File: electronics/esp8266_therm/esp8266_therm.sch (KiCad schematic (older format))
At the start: 20 parts, among them J1 CONN_01X02, J2 CONN_01X03, J3 CONN_01X03, J4 CONN_01X02, J5 CONN_01X08, J6 CONN_01X08, J7 CONN_01X02, J8 CONN_01X06, M1 BMP180_Breakout, Q1 Q_PMOS_GSD, SW1 SW_SPST, SW2 SW_SPST, U1 ESP-12E, U2 MCP1703A-3302/MB

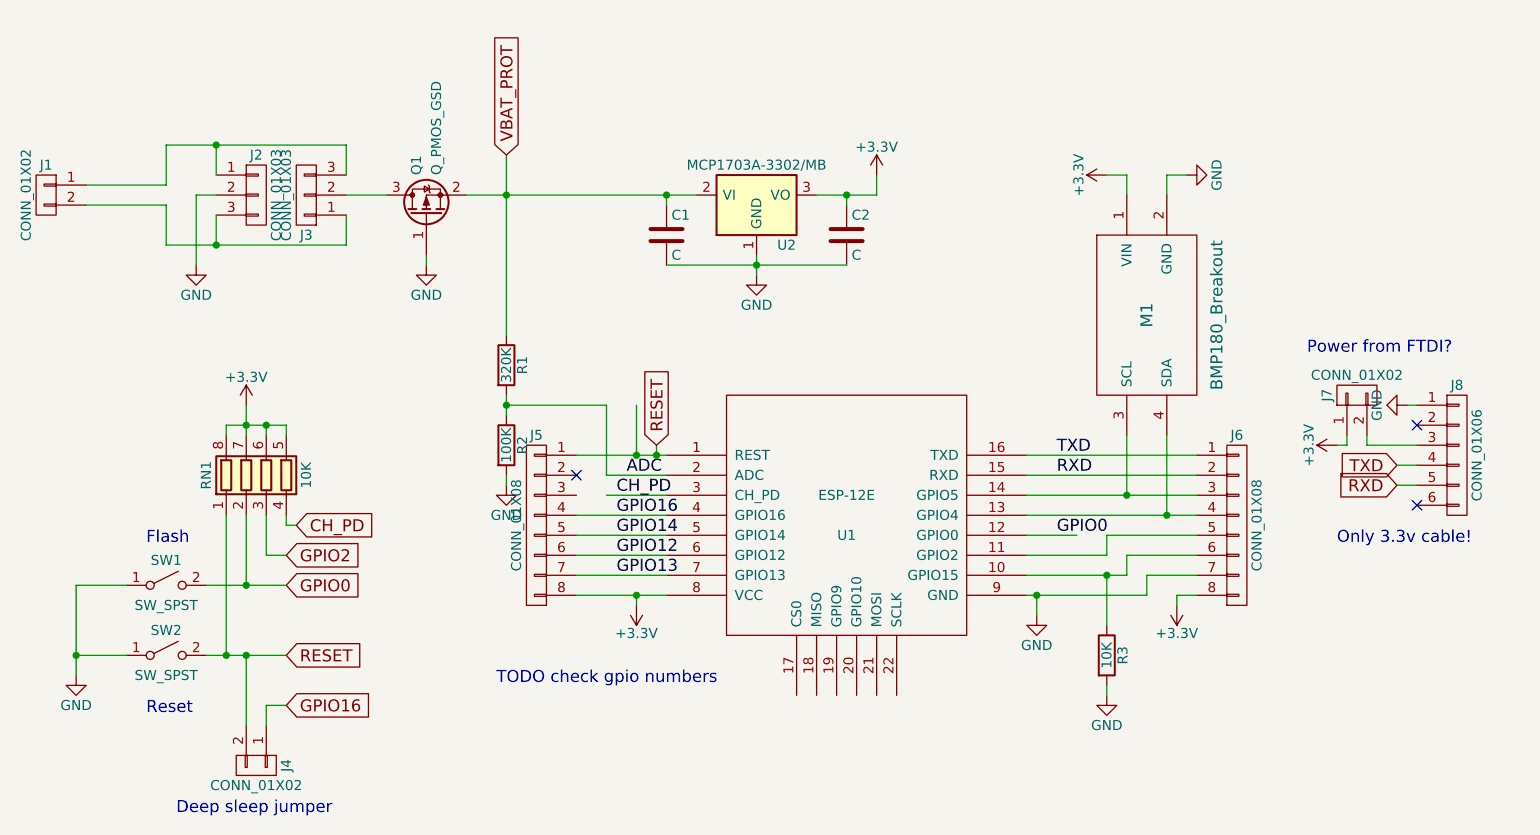
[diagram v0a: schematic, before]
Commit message: Update pinout on board to match D1 mini
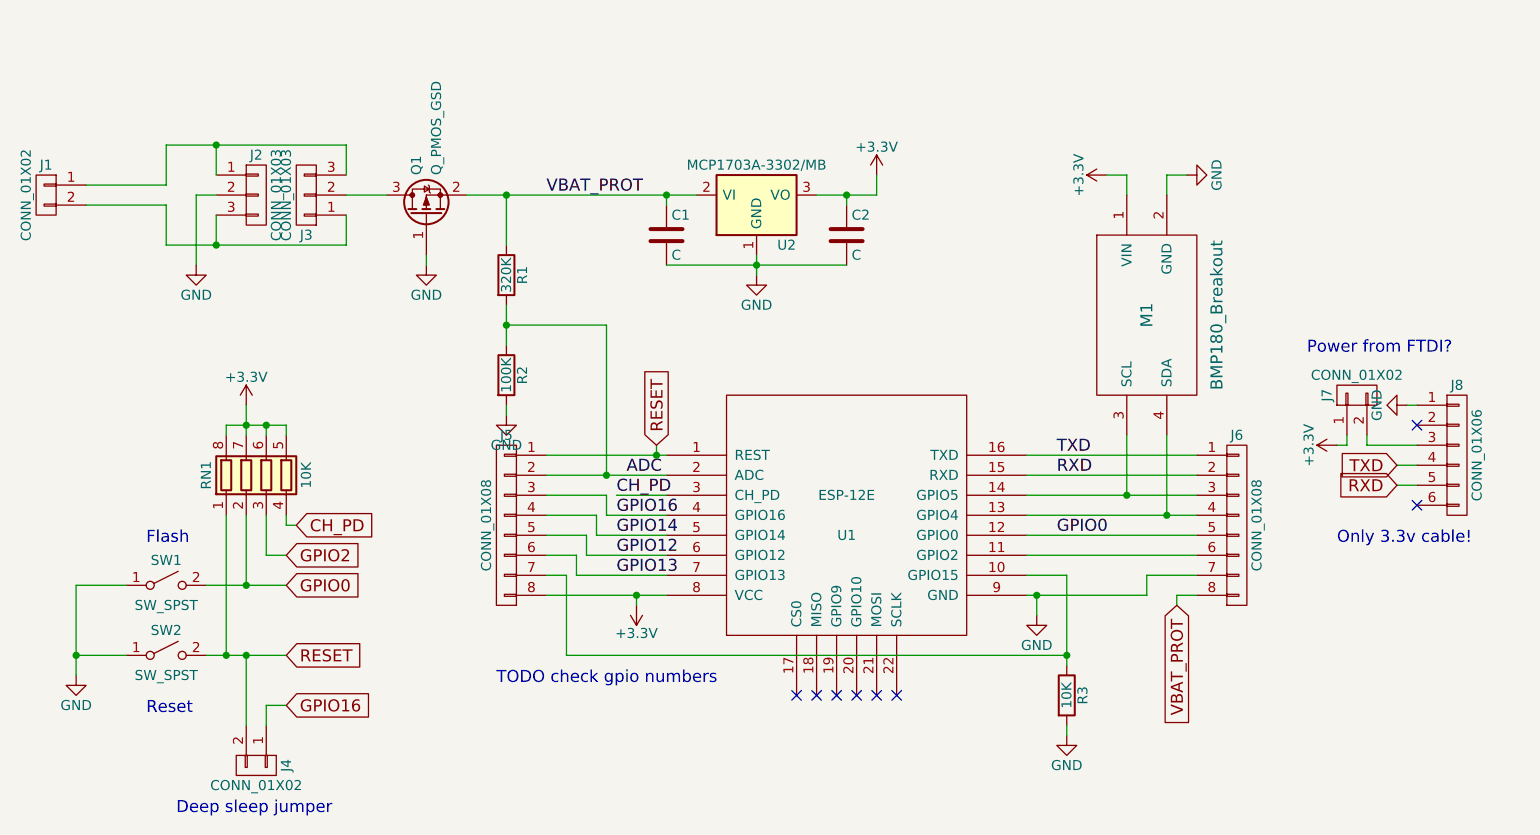
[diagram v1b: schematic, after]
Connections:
- wire segments 88 -> 94
- no-connect marks 3 -> 8
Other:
- moved on the sheet: J5, R1, R2, R3
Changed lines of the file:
@@
 L R R1
 U 1 1 5960122C
-P 5150 3600
-F 0 "R1" V 5230 3600 50  0000 C CNN
-F 1 "320K" V 5150 3600 50  0000 C CNN
-F 2 "Resistors_SMD:R_0603_HandSoldering" V 5080 3600 50  0001 C CNN
-F 3 "" H 5150 3600 50  0001 C CNN
-	1    5150 3600
+P 5150 3150
+F 0 "R1" V 5230 3150 50  0000 C CNN
+F 1 "320K" V 5150 3150 50  0000 C CNN
+F 2 "Resistors_SMD:R_0603_HandSoldering" V 5080 3150 50  0001 C CNN
+F 3 "" H 5150 3150 50  0001 C CNN
+	1    5150 3150
 	1    0    0    -1
 $EndComp
@@
 L R R2
 U 1 1 59601270
-P 5150 4000
-F 0 "R2" V 5230 4000 50  0000 C CNN
-F 1 "100K" V 5150 4000 50  0000 C CNN
-F 2 "Resistors_SMD:R_0603_HandSoldering" V 5080 4000 50  0001 C CNN
-F 3 "" H 5150 4000 50  0001 C CNN
-	1    5150 4000
+P 5150 3650
+F 0 "R2" V 5230 3650 50  0000 C CNN
+F 1 "100K" V 5150 3650 50  0000 C CNN
+F 2 "Resistors_SMD:R_0603_HandSoldering" V 5080 3650 50  0001 C CNN
+F 3 "" H 5150 3650 50  0001 C CNN
+	1    5150 3650
 	1    0    0    -1
 $EndComp
@@
 L GND #PWR07
 U 1 1 596012FB
-P 5150 4200
-F 0 "#PWR07" H 5150 3950 50  0001 C CNN
-F 1 "GND" H 5150 4050 50  0000 C CNN
-F 2 "" H 5150 4200 50  0001 C CNN
-F 3 "" H 5150 4200 50  0001 C CNN
-	1    5150 4200
+P 5150 3850
+F 0 "#PWR07" H 5150 3600 50  0001 C CNN
+F 1 "GND" H 5150 3700 50  0000 C CNN
+F 2 "" H 5150 3850 50  0001 C CNN
+F 3 "" H 5150 3850 50  0001 C CNN
+	1    5150 3850
 	1    0    0    -1
 $EndComp
@@
 L CONN_01X08 J5
 U 1 1 59602C27
-P 5300 4400
-F 0 "J5" H 5300 4850 50  0000 C CNN
-F 1 "CONN_01X08" V 5400 4400 50  0000 C CNN
-F 2 "Pin_Headers:Pin_Header_Straight_1x08_Pitch2.54mm" H 5300 4400 50  0001 C CNN
-F 3 "" H 5300 4400 50  0001 C CNN
-	1    5300 4400
+P 5150 4400
+F 0 "J5" H 5150 4850 50  0000 C CNN
+F 1 "CONN_01X08" V 5250 4400 50  0000 C CNN
+F 2 "Pin_Headers:Pin_Header_Straight_1x08_Pitch2.54mm" H 5150 4400 50  0001 C CNN
+F 3 "" H 5150 4400 50  0001 C CNN
+	1    5150 4400
 	-1   0    0    -1
 $EndComp
@@
 	1    0    0    -1
 $EndComp
-$Comp
-L +3.3V #PWR011
-U 1 1 59603692
-P 8500 4800
-F 0 "#PWR011" H 8500 4650 50  0001 C CNN
-F 1 "+3.3V" H 8500 4940 50  0000 C CNN
-F 2 "" H 8500 4800 50  0001 C CNN
-F 3 "" H 8500 4800 50  0001 C CNN
-	1    8500 4800
-	-1   0    0    1
-$EndComp
 Text Notes 3350 5350 0    60   ~ 0
 Reset
@@
 $EndComp
 $Comp
-L GND #PWR012
+L GND #PWR011
 U 1 1 59604130
 P 9650 3800
-F 0 "#PWR012" H 9650 3550 50  0001 C CNN
+F 0 "#PWR011" H 9650 3550 50  0001 C CNN
 F 1 "GND" H 9650 3650 50  0000 C CNN
 F 2 "" H 9650 3800 50  0001 C CNN
@@
 $EndComp
 $Comp
-L +3.3V #PWR013
+L +3.3V #PWR012
 U 1 1 5960417A
 P 9300 4000
-F 0 "#PWR013" H 9300 3850 50  0001 C CNN
+F 0 "#PWR012" H 9300 3850 50  0001 C CNN
 F 1 "+3.3V" H 9300 4140 50  0000 C CNN
 F 2 "" H 9300 4000 50  0001 C CNN
@@
 RXD
 $Comp
-L +3.3V #PWR014
+L +3.3V #PWR013
 U 1 1 5960556B
 P 3850 3800
-F 0 "#PWR014" H 3850 3650 50  0001 C CNN
+F 0 "#PWR013" H 3850 3650 50  0001 C CNN
 F 1 "+3.3V" H 3850 3940 50  0000 C CNN
 F 2 "" H 3850 3800 50  0001 C CNN
@@
 Text GLabel 4050 5300 2    60   Input ~ 0
 GPIO16
-NoConn ~ 5500 4150
 Text Notes 5100 5200 0    60   ~ 0
 TODO check gpio numbers
@@
 GPIO0
 Wire Wire Line
-	5500 4750 5950 4750
-Wire Wire Line
 	8250 2750 8250 2650
 Wire Wire Line
@@
 Connection ~ 5950 2750
 Wire Wire Line
-	5150 3750 5150 3850
-Connection ~ 5150 3800
-Wire Wire Line
-	5150 4200 5150 4150
+	5150 3300 5150 3500
+Connection ~ 5150 3400
+Wire Wire Line
+	5150 3850 5150 3800
 Wire Wire Line
 	3700 2750 3600 2750
@@
 Connection ~ 5150 2750
 Wire Wire Line
-	5500 4050 5950 4050
-Wire Wire Line
-	5800 4050 5800 3800
+	5350 4050 5950 4050
 Wire Wire Line
 	5900 4000 5900 4050
@@
 	5800 4750 5800 4800
 Connection ~ 5800 4750
-Wire Wire Line
-	5500 4650 5950 4650
-Wire Wire Line
-	5950 4550 5500 4550
-Wire Wire Line
-	5500 4450 5950 4450
-Wire Wire Line
-	5950 4350 5500 4350
 Connection ~ 7800 4750
 Wire Wire Line
@@
 	7750 4350 8600 4350
 Wire Wire Line
-	7750 4550 8150 4550
-Wire Wire Line
-	8150 4550 8150 4450
-Wire Wire Line
-	8150 4450 8600 4450
-Wire Wire Line
-	8600 4550 8250 4550
-Wire Wire Line
-	8250 4550 8250 4650
-Wire Wire Line
-	8250 4650 7750 4650
+	7750 4550 8600 4550
 Wire Wire Line
 	8600 4650 8350 4650
@@
 	8350 4750 7750 4750
 Wire Wire Line
-	8600 4750 8500 4750
-Wire Wire Line
 	8500 4750 8500 4800
-Connection ~ 5800 4050
-Wire Wire Line
-	5650 4150 5950 4150
-Wire Wire Line
-	5650 3800 5650 4150
-Wire Wire Line
-	5150 3800 5650 3800
-Wire Wire Line
-	5150 2550 5150 3450
+Wire Wire Line
+	5350 4150 5950 4150
+Wire Wire Line
+	5650 3400 5650 4150
+Wire Wire Line
+	5150 3400 5650 3400
 Wire Wire Line
 	9650 3800 9700 3800
@@
 	3850 4350 3850 4700
 Connection ~ 3850 4700
-Wire Wire Line
-	5650 4250 5950 4250
 Wire Wire Line
 	4100 4400 4050 4400
@@
 L R R3
 U 1 1 59607D48
-P 8150 5050
-F 0 "R3" V 8230 5050 50  0000 C CNN
-F 1 "10K" V 8150 5050 50  0000 C CNN
-F 2 "Resistors_SMD:R_0603_HandSoldering" V 8080 5050 50  0001 C CNN
-F 3 "" H 8150 5050 50  0001 C CNN
-	1    8150 5050
-	1    0    0    -1
-$EndComp
-Wire Wire Line
-	8150 4650 8150 4900
-Connection ~ 8150 4650
-$Comp
-L GND #PWR015
+P 7950 5250
+F 0 "R3" V 8030 5250 50  0000 C CNN
+F 1 "10K" V 7950 5250 50  0000 C CNN
+F 2 "Resistors_SMD:R_0603_HandSoldering" V 7880 5250 50  0001 C CNN
+F 3 "" H 7950 5250 50  0001 C CNN
+	1    7950 5250
+	1    0    0    -1
+$EndComp
+$Comp
+L GND #PWR014
 U 1 1 59607E1E
-P 8150 5250
-F 0 "#PWR015" H 8150 5000 50  0001 C CNN
-F 1 "GND" H 8150 5100 50  0000 C CNN
-F 2 "" H 8150 5250 50  0001 C CNN
-F 3 "" H 8150 5250 50  0001 C CNN
-	1    8150 5250
-	1    0    0    -1
-$EndComp
-Wire Wire Line
-	8150 5200 8150 5250
-Text GLabel 5150 2550 1    60   Input ~ 0
-VBAT_PROT
-Wire Wire Line
-	7750 4450 8000 4450
+P 7950 5450
+F 0 "#PWR014" H 7950 5200 50  0001 C CNN
+F 1 "GND" H 7950 5300 50  0000 C CNN
+F 2 "" H 7950 5450 50  0001 C CNN
+F 3 "" H 7950 5450 50  0001 C CNN
+	1    7950 5450
+	1    0    0    -1
+$EndComp
+Wire Wire Line
+	7950 5400 7950 5450
+Wire Wire Line
+	7750 4450 8600 4450
 Text Label 7900 4450 0    60   ~ 0
 GPIO0
+Text Label 5350 2750 0    60   ~ 0
+VBAT_PROT
+Wire Wire Line
+	5150 2750 5150 3000
+Connection ~ 5650 4150
+Wire Wire Line
+	5700 4250 5950 4250
+Wire Wire Line
+	5350 4250 5650 4250
+Wire Wire Line
+	5650 4250 5650 4350
+Wire Wire Line
+	5650 4350 5950 4350
+Wire Wire Line
+	5950 4450 5600 4450
+Wire Wire Line
+	5600 4450 5600 4350
+Wire Wire Line
+	5600 4350 5350 4350
+Wire Wire Line
+	5950 4550 5550 4550
+Wire Wire Line
+	5550 4550 5550 4450
+Wire Wire Line
+	5550 4450 5350 4450
+Wire Wire Line
+	5950 4650 5500 4650
+Wire Wire Line
+	5500 4650 5500 4550
+Wire Wire Line
+	5500 4550 5350 4550
+Wire Wire Line
+	5950 4750 5350 4750
+Wire Wire Line
+	5350 4650 5450 4650
+Wire Wire Line
+	5450 4650 5450 5050
+Wire Wire Line
+	5450 5050 7950 5050
+Wire Wire Line
+	7950 4650 7950 5100
+Connection ~ 7950 5050
+Wire Wire Line
+	7950 4650 7750 4650
+Wire Wire Line
+	8600 4750 8500 4750
+Text GLabel 8500 4800 3    60   Input ~ 0
+VBAT_PROT
+NoConn ~ 6600 5250
+NoConn ~ 6700 5250
+NoConn ~ 6800 5250
+NoConn ~ 6900 5250
+NoConn ~ 7000 5250
+NoConn ~ 7100 5250
 $EndSCHEMATC
